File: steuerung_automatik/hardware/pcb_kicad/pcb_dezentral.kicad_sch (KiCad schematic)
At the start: 37 parts, among them J101 USB_C_Receptacle_USB2.0, J102 weidmueller_SL5.08HC-06-90, J103 weidmueller_SL5.08HC-10-90, SW101 SW_MEC_5E, SW102 SW_MEC_5E, U101 RP2040, U102 W25Q128JVS, U103 SP3485EN-L/TR, U104 AMS1117-3.3, Y101 Crystal_GND24_Small

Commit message: Schema dezentral komplett
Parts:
- removed C101, C102, C105, C106, C109, C110, C111, C112, C113, C114: 100n, Capacitor_SMD:C_0402_1005Metric_Pad0.74x0.62mm_HandSolder, symbol 00_project_library:C
- removed C103, C104: 1u, Capacitor_SMD:C_0402_1005Metric_Pad0.74x0.62mm_HandSolder, symbol 00_project_library:C
- removed C107, C108: 30p, Capacitor_SMD:C_0402_1005Metric, symbol 00_project_library:C
- removed C115, C116: 10u, Capacitor_SMD:C_0603_1608Metric, symbol 00_project_library:C
- removed D101: LED GREEN, 00_project_library:LED_0603_1608Metric, symbol 00_project_library:LED GREEN
- removed J101: USB_C_Receptacle_USB2.0, 00_project_library:USB_C_Receptacle_Palconn_UTC16-G, symbol 00_project_library:USB_C_Receptacle_USB2.0
- removed R101, R102: 5.1K, Resistor_SMD:R_0402_1005Metric_Pad0.72x0.64mm_HandSolder, symbol Device:R
- removed R103, R104: 27R, Resistor_SMD:R_0402_1005Metric_Pad0.72x0.64mm_HandSolder, symbol Device:R
- removed R105, R107: 10K, Resistor_SMD:R_0402_1005Metric_Pad0.72x0.64mm_HandSolder, symbol Device:R
- removed R106: 470R, Resistor_SMD:R_0402_1005Metric_Pad0.72x0.64mm_HandSolder, symbol Device:R
- removed R108: 1k, Resistor_SMD:R_0402_1005Metric_Pad0.72x0.64mm_HandSolder, symbol Device:R
- removed SW101, SW102: SW_MEC_5E, 00_project_library:SW_TS-1187A-B-A-B, symbol 00_project_library:SW_MEC_5E
- removed TP101: TestPoint, TestPoint:TestPoint_Pad_D2.5mm, symbol Connector:TestPoint
- removed U101: RP2040, 00_project_library:RP2040-QFN-56, symbol 00_project_library:RP2040
- removed U102: W25Q128JVS, 00_project_library:SOIC-8_5.23x5.23mm_P1.27mm, symbol 00_project_library:W25Q128JVS
- removed U104: AMS1117-3.3, 00_project_library:SOT-223-3_TabPin2, symbol 00_project_library:AMS1117-3.3
- removed Y101: Crystal_GND24_Small, 00_project_library:Crystal_SMD_3225-4Pin_3.2x2.5mm, symbol 00_project_library:Crystal_GND24_Small
- added C1: 4u7 50V, Diode_SMD:D_1206_3216Metric, symbol Device:C
- added C2, C3, C5, C6: 100n 50V, Diode_SMD:D_0805_2012Metric, symbol Device:C
- added C4: 10u 25V, Diode_SMD:D_0805_2012Metric, symbol Device:C
- added D1, D10, D11, D12, D13, D14, D15, D16, D19, D2, D20, D24, D25, D3, D4, D5, D6, D7, D8, D9: B5819W SL, Diode_SMD:D_SOD-123, symbol Device:D_Schottky
- added D17: SMBJ30A, Diode_SMD:D_SMA, symbol Diode:SMAJ64A
- added D18: LED WHITE, 00_project_library:LED_0603_1608Metric, symbol 00_project_library:LED WHITE
- added D21, D22, D23: SMBJ6.5CA, Diode_SMD:D_SMB, symbol Diode:SMAJ64CA
- added L1: 22uH, 00_project_library:L_MODBUS, symbol Device:L
- added Q1: AO3400A, Package_TO_SOT_SMD:SOT-23, symbol Transistor_FET:AO3400A
- added R1, R2, R3, R4, R5, R6, R7, R8: 4k7, Resistor_SMD:R_0402_1005Metric_Pad0.72x0.64mm_HandSolder, symbol Device:R
- added R10, R13: 10k, Resistor_SMD:R_0402_1005Metric_Pad0.72x0.64mm_HandSolder, symbol Device:R
- added R11: 100k, Resistor_SMD:R_0402_1005Metric_Pad0.72x0.64mm_HandSolder, symbol Device:R
- added R12: 56k, Resistor_SMD:R_0402_1005Metric_Pad0.72x0.64mm_HandSolder, symbol Device:R
- added R9: 470, Resistor_SMD:R_0402_1005Metric_Pad0.72x0.64mm_HandSolder, symbol Device:R
- added SW1: dip_switch_SPST16, 00_project_library:dip_switch_SPST16, symbol 00_project_library:dip_switch_SPST16
- added U2: AOZ1282CI, Package_TO_SOT_SMD:SOT-23-6, symbol Regulator_Switching:AOZ1282CI
- renumbered HOLDER101 to HOLDER1, J102 to J1, J103 to J2, U103 to U1
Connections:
- net +3V3: now also J2.9, C6.2, D1.1 (K), D11.1 (K), D13.1 (K), D15.1 (K), D3.1 (K), D5.1 (K), D7.1 (K), D9.1 (K), R1.1, R2.1, R3.1, R4.1, R5.1, R6.1, R7.1, R8.1, SW1.1-1, SW1.2-1, SW1.3-1, SW1.4-1, SW1.5-1, SW1.6-1, SW1.7-1, SW1.8-1
- net +5V: now also D25.1 (K)
- net GND: now also J1.3, J2.10, U1.5 (GND), C1.2, C2.2, C4.1, C5.1, C6.1, D10.2 (A), D12.2 (A), D14.2 (A), D16.2 (A), D17.2 (A2), D2.2 (A), D21.2 (A2), D23.1 (A1), D24.2 (A), D4.2 (A), D6.2 (A), D8.2 (A), Q1.2 (S), R10.2, R13.2, R9.2, U2.2 (GND)
- net MODBUS_RO: now reaches U1.1 (RO)
- net MODBUS_DE: now reaches U1.2 (~{RE})
- net MODBUS_DE: now also U1.3 (DE)
- net MODBUS_DI: now reaches U1.4 (DI)
- net 485_A: now reaches U1.6 (A)
- net 485_A: now also J1.1, D21.1 (A1), D22.2 (A2)
- net 485_B: now reaches U1.7 (B)
- net 485_B: now also J1.2, D22.1 (A1), D23.2 (A2)
- net +3.3V: now reaches U1.8 (VCC)
- net ds_0: now reaches J2.1
- net ds_0: now also D1.2 (A), D2.1 (K), R1.2
- net ds_1: now reaches J2.2
- net ds_1: now also D3.2 (A), D4.1 (K), R2.2
- net ds_2: now reaches J2.3
- net ds_2: now also D5.2 (A), D6.1 (K), R3.2
- net ds_3: now reaches J2.4
- net ds_3: now also D7.2 (A), D8.1 (K), R4.2
- net ds_4: now reaches J2.5
- net ds_4: now also D10.1 (K), D9.2 (A), R5.2
- net ds_5: now reaches J2.6
- net ds_5: now also D11.2 (A), D12.1 (K), R6.2
- net ds_6: now reaches J2.7
- net ds_6: now also D13.2 (A), D14.1 (K), R7.2
- net ds_7: now reaches J2.8
- net ds_7: now also D15.2 (A), D16.1 (K), R8.2
- net 485_24V: now reaches J1.4
- net 485_24V: now also J1.5, D17.1 (A1), D19.2 (A), D20.1 (K)
- net rel_n: now reaches J1.6
- net rel_n: now also D20.2 (A), Q1.3 (D)
- new net: C1.1, C2.1, D19.1 (K), R11.1, U2.5 (VIN)
- new net: R12.1, R13.1, U2.3 (FB)
- new net: D18.1 (K), R9.1
- new net: C4.2, C5.2, D25.2 (A), L1.2, R12.2
- new net: R11.2, U2.4 (EN)
- new net: C3.2, D24.1 (K), L1.1, U2.6 (LX)
- new net: C3.1, U2.1 (BST)
- new net modbus_addr_0: SW1.1
- new net modbus_addr_1: SW1.2
- new net modbus_addr_2: SW1.3
- new net modbus_addr_3: SW1.4
- new net modbus_addr_4: SW1.5
- new net modbus_addr_5: SW1.6
- new net modbus_addr_6: SW1.7
- new net modbus_addr_7: SW1.8
- new net rel: D18.2 (A), Q1.1 (G), R10.1
- no-connect marks 34 -> 0
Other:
- added sheet cpu (pcb_dezentral_cpu.kicad_sch)
- note added: "5.3V"
- note added: "Mechanics"
- note removed: "Bypass Capacitors"
- note removed: "C1, C2 = 2*CL - 2*Cs CL = 20pF, Cs can be ~5pF"
- note removed: "Crystal"
- note removed: "Flash Memory"
- note removed: "Main Regulator"
- note removed: "Make sure 27R are close to RP2040"
- note removed: "Mounting Hole"
- note removed: "Place 1uF close to pin 44"
- note removed: "Place 1uF close to pin 45"
- note removed: "Power LED"
- note removed: "RP2040"
- note removed: "Reset"
- note removed: "USB Type-C"
- title: Heizung Pünterswis - pcb_zentral -> Heizung Pünterswis - pcb_dezentral
- moved on the sheet: J1, J2, U1

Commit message: Schema dezentral komplett
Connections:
- net +3.3V is gone; now on net +3V3: U1.8 (VCC)
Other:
- moved on the sheet: C6, D10, D12, D14, D16, D17, D2, D4, D6, D8

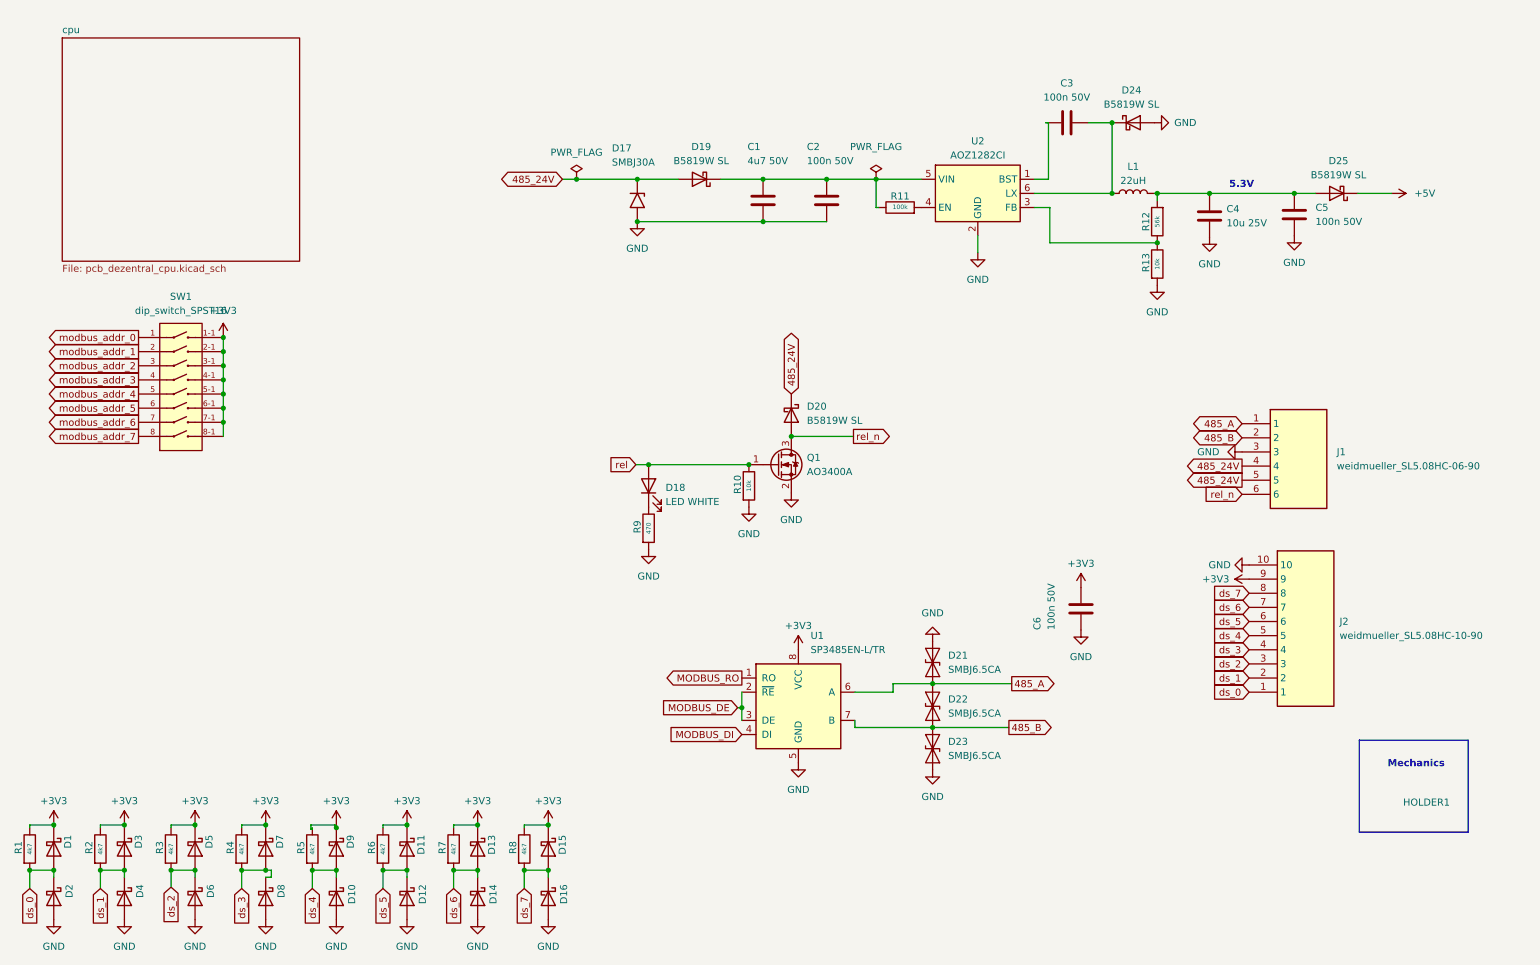
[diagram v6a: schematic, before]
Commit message: Schema bereinigt
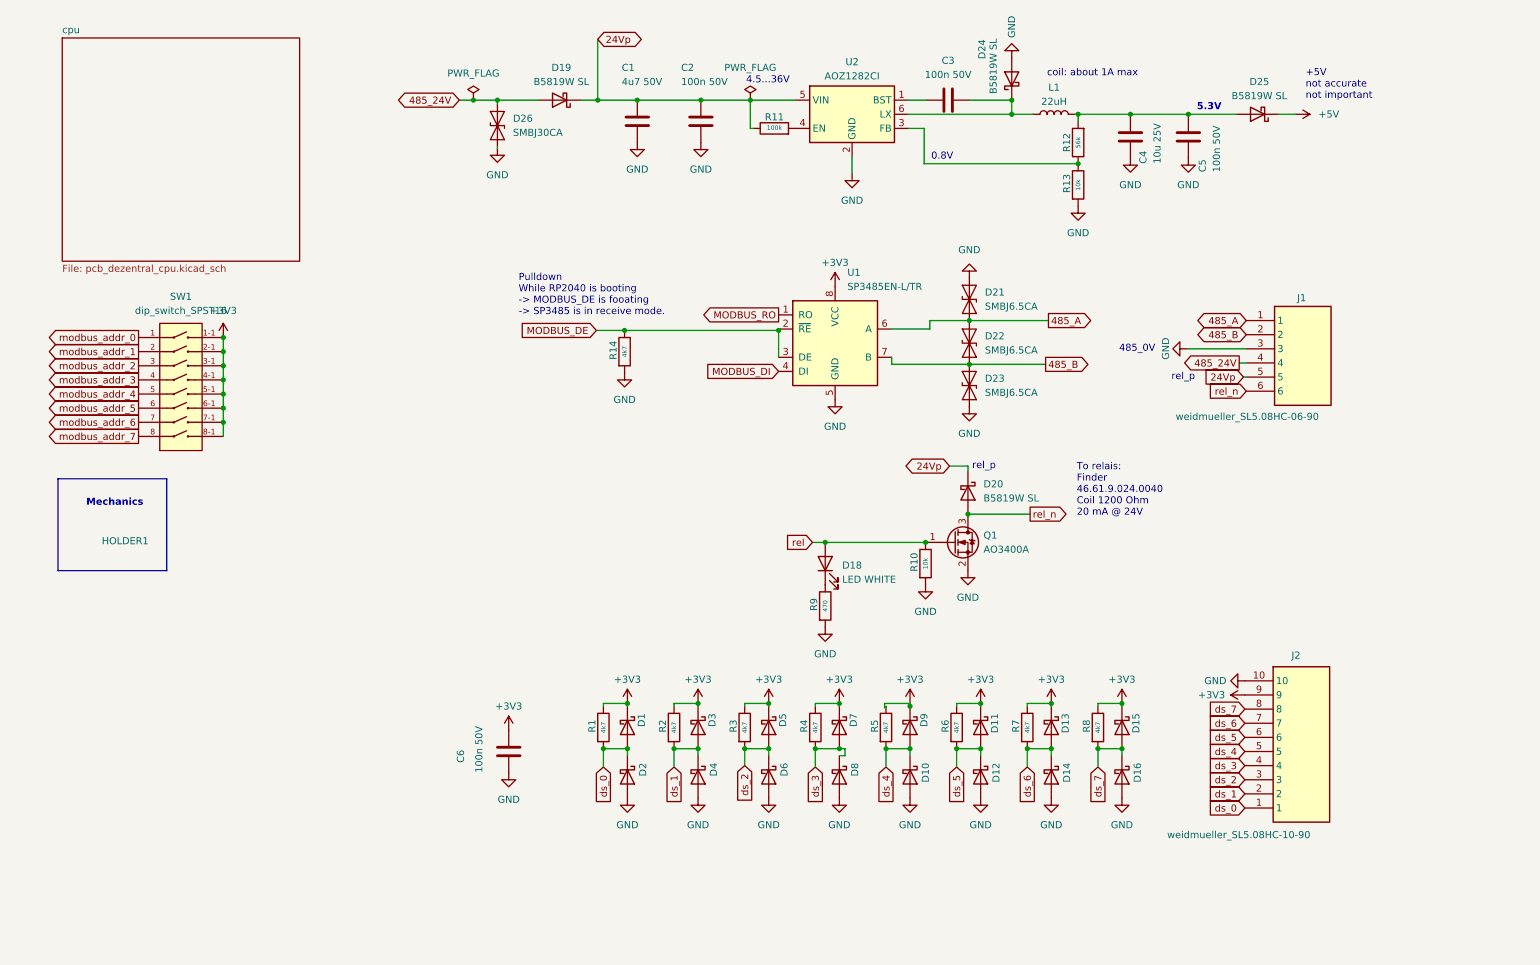
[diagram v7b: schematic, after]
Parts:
- removed D17: SMBJ30A, Diode_SMD:D_SMA, symbol Diode:SMAJ64A
- added D26: SMBJ30CA, Diode_SMD:D_SMB, symbol Diode:SMAJ64CA
- added R14: 4k7, Resistor_SMD:R_0402_1005Metric_Pad0.72x0.64mm_HandSolder, symbol Device:R
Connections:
- net 485_24V: now also D26.2 (A2); no longer D20.1 (K), J1.5
- net GND: now also D26.1 (A1), R14.2
- net MODBUS_DE: now also R14.1
- net 24Vp: now reaches C1.1, C2.1, D19.1 (K), R11.1, U2.5 (VIN)
- net 24Vp: now also D20.1 (K), J1.5
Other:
- note added: "+5V not accurate not important"
- note added: "0.8V"
- note added: "4.5...36V"
- note added: "485_0V"
- note added: "Pulldown While RP2040 is booting -> MODBUS_DE is fooating -> SP3485 is in receive mode."
- note added: "To relais: Finder 46.61.9.024.0040 Coil 1200 Ohm 20 mA @ 24V"
- note added: "coil: about 1A max"
- note added: "rel_p"
- moved on the sheet: C1, C2, C3, C4, C5, C6, D1, D10, D11, D12, D13, D14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

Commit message: Anpassungen von Peter
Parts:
- added D17: LED RED, 00_project_library:LED_0603_1608Metric, symbol 00_project_library:LED RED
- added D27: LED BLUE, 00_project_library:LED_0603_1608Metric, symbol 00_project_library:LED BLUE
- added R15, R16: 470R, Resistor_SMD:R_0402_1005Metric_Pad0.72x0.64mm_HandSolder, symbol Device:R
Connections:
- net GND: now also R15.1, R16.1
- new net: D17.1 (K), R15.2
- new net: D27.2 (A), R16.2
- new net modbus_led: D17.2 (A), D27.1 (K)
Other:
- note added: "Modbus LED"
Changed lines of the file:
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@@
     (stroke (width 0) (type default))
+  )
+  (wire (pts (xy 49.53 151.638) (xy 53.34 151.638))
+    (stroke (width 0) (type solid))
   )
   (wire (pts (xy 52.578 82.042) (xy 52.578 84.582))
@@
     (stroke (width 0) (type default))
   )
+  (wire (pts (xy 60.96 151.638) (xy 62.23 151.638))
+    (stroke (width 0) (type solid))
+  )
   (wire (pts (xy 52.578 74.422) (xy 52.578 76.962))
     (stroke (width 0) (type default))
@@
     (stroke (width 0) (type default))
   )
+  (wire (pts (xy 49.53 162.052) (xy 53.34 162.052))
+    (stroke (width 0) (type solid))
+  )
   (wire (pts (xy 101.854 40.132) (xy 101.854 40.386))
     (stroke (width 0) (type default))
@@
     (stroke (width 0) (type default))
   )
+  (wire (pts (xy 60.96 162.052) (xy 62.23 162.052))
+    (stroke (width 0) (type solid))
+  )
   (wire (pts (xy 179.578 71.374) (xy 186.69 71.374))
     (stroke (width 0) (type default))
@@
     (stroke (width 0) (type default))
   )
+  (wire (pts (xy 39.37 162.052) (xy 41.91 162.052))
+    (stroke (width 0) (type default))
+  )
   (wire (pts (xy 119.888 20.828) (xy 119.888 31.75))
     (stroke (width 0) (type default))
@@
     (stroke (width 0) (type default))
   )
+  (wire (pts (xy 39.37 151.638) (xy 41.91 151.638))
+    (stroke (width 0) (type default))
+  )
   (wire (pts (xy 52.578 79.502) (xy 52.578 82.042))
     (stroke (width 0) (type default))
@@
     (stroke (width 0) (type default))
   )
+  (rectangle (start 23.876 139.192) (end 69.088 165.608)
+    (stroke (width 0) (type default))
+    (fill (type none))
+  )
   (rectangle (start 22.86 99.822) (end 42.418 116.332)
     (stroke (width 0) (type default))
@@
   )
   (text "Mechanics" (at 27.94 104.902 0)
+    (effects (font (size 1.27 1.27) (thickness 0.254) bold) (justify left bottom))
+  )
+  (text "Modbus LED" (at 30.48 144.526 0)
     (effects (font (size 1.27 1.27) (thickness 0.254) bold) (justify left bottom))
   )
@@
   (text "0.8V" (at 179.832 42.672 0)
     (effects (font (size 1.27 1.27)) (justify left bottom))
+  )
+  (global_label "modbus_led" (shape output) (at 39.37 151.638 180) (fields_autoplaced)
+    (effects (font (size 1.27 1.27)) (justify right))
+    (property "Intersheetrefs" "${INTERSHEET_REFS}" (at 25.1019 151.638 0)
+      (effects (font (size 1.27 1.27)) (justify right) hide)
+    )
   )
   (global_label "modbus_addr_3" (shape output) (at 37.338 82.042 180) (fields_autoplaced)
@@
     )
   )
+  (global_label "modbus_led" (shape output) (at 39.37 162.052 180) (fields_autoplaced)
+    (effects (font (size 1.27 1.27)) (justify right))
+    (property "Intersheetrefs" "${INTERSHEET_REFS}" (at 25.1019 162.052 0)
+      (effects (font (size 1.27 1.27)) (justify right) hide)
+    )
+  )
   (global_label "modbus_addr_5" (shape output) (at 37.338 87.122 180) (fields_autoplaced)
     (effects (font (size 1.27 1.27)) (justify right))
@@
     )
   )
+  (symbol (lib_id "power:GND") (at 62.23 162.052 90) (unit 1)
+    (in_bom yes) (on_board yes) (dnp no)
+    (property "Reference" "#PWR042" (at 68.58 162.052 0)
+      (effects (font (size 0.8 0.8)) hide)
+    )
+    (property "Value" "GND" (at 65.8622 162.179 0)
+      (effects (font (size 0.8 0.8)))
+    )
+    (property "Footprint" "" (at 62.23 162.052 0)
+      (effects (font (size 0.8 0.8)) hide)
+    )
+    (property "Datasheet" "" (at 62.23 162.052 0)
+      (effects (font (size 0.8 0.8)) hide)
+    )
+    (pin "1")
+    (instances
+      (project "pcb_dezentral"
+        (path "/35c47459-45a7-4753-acae-c8b47e7575e1"
+          (reference "#PWR042") (unit 1)
+        )
+        (path "/35c47459-45a7-4753-acae-c8b47e7575e1/24d7d496-8920-4421-a637-0c9bf263a085"
+          (reference "#PWR0913") (unit 1)
+        )
+      )
+    )
+  )
   (symbol (lib_id "power:GND") (at 178.816 118.872 0) (unit 1)
     (in_bom yes) (on_board yes) (dnp no) (fields_autoplaced)
@@
         (path "/35c47459-45a7-4753-acae-c8b47e7575e1"
           (reference "#PWR020") (unit 1)
+        )
+      )
+    )
+  )
+  (symbol (lib_id "Device:R") (at 57.15 151.638 270) (unit 1)
+    (in_bom yes) (on_board yes) (dnp no)
+    (property "Reference" "R15" (at 57.15 153.67 90)
+      (effects (font (size 1.27 1.27)))
+    )
+    (property "Value" "470R" (at 57.15 151.7396 90)
+      (effects (font (size 0.8 0.8)))
+    )
+    (property "Footprint" "Resistor_SMD:R_0402_1005Metric_Pad0.72x0.64mm_HandSolder" (at 57.15 149.86 90)
+      (effects (font (size 1.27 1.27)) hide)
+    )
+    (property "Datasheet" "~" (at 57.15 151.638 0)
+      (effects (font (size 1.27 1.27)) hide)
+    )
+    (pin "1")
+    (pin "2")
+    (instances
+      (project "pcb_dezentral"
+        (path "/35c47459-45a7-4753-acae-c8b47e7575e1"
+          (reference "R15") (unit 1)
+        )
+        (path "/35c47459-45a7-4753-acae-c8b47e7575e1/24d7d496-8920-4421-a637-0c9bf263a085"
+          (reference "R905") (unit 1)
         )
       )
@@
         (path "/35c47459-45a7-4753-acae-c8b47e7575e1"
           (reference "#PWR014") (unit 1)
+        )
+      )
+    )
+  )
+  (symbol (lib_id "00_project_library:LED RED") (at 45.72 151.638 180) (unit 1)
+    (in_bom yes) (on_board yes) (dnp no) (fields_autoplaced)
+    (property "Reference" "D17" (at 47.3075 144.526 0)
+      (effects (font (size 1.27 1.27)))
+    )
+    (property "Value" "LED RED" (at 47.3075 147.066 0)
+      (effects (font (size 1.27 1.27)))
+    )
+    (property "Footprint" "00_project_library:LED_0603_1608Metric" (at 45.72 151.638 0)
+      (effects (font (size 1.27 1.27)) hide)
+    )
+    (property "Datasheet" "~" (at 45.72 151.638 0)
+      (effects (font (size 1.27 1.27)) hide)
+    )
+    (property "JLC" "C2286" (at 45.72 151.638 0)
+      (effects (font (size 1.27 1.27)) hide)
+    )
+    (pin "1")
+    (pin "2")
+    (instances
+      (project "pcb_dezentral"
+        (path "/35c47459-45a7-4753-acae-c8b47e7575e1"
+          (reference "D17") (unit 1)
         )
       )
@@
         (path "/35c47459-45a7-4753-acae-c8b47e7575e1"
           (reference "D1") (unit 1)
+        )
+      )
+    )
+  )
+  (symbol (lib_id "00_project_library:LED BLUE") (at 45.72 162.052 0) (unit 1)
+    (in_bom yes) (on_board yes) (dnp no) (fields_autoplaced)
+    (property "Reference" "D27" (at 44.1325 155.956 0)
+      (effects (font (size 1.27 1.27)))
+    )
+    (property "Value" "LED BLUE" (at 44.1325 158.496 0)
+      (effects (font (size 1.27 1.27)))
+    )
+    (property "Footprint" "00_project_library:LED_0603_1608Metric" (at 45.72 162.052 0)
+      (effects (font (size 1.27 1.27)) hide)
+    )
+    (property "Datasheet" "~" (at 45.72 162.052 0)
+      (effects (font (size 1.27 1.27)) hide)
+    )
+    (property "JLC" "C189307" (at 45.72 162.052 0)
+      (effects (font (size 1.27 1.27)) hide)
+    )
+    (pin "1")
+    (pin "2")
+    (instances
+      (project "pcb_dezentral"
+        (path "/35c47459-45a7-4753-acae-c8b47e7575e1"
+          (reference "D27") (unit 1)
         )
       )
@@
         )
       )
+    )
+  )
+  (symbol (lib_id "power:GND") (at 62.23 151.638 90) (unit 1)
+    (in_bom yes) (on_board yes) (dnp no)
+    (property "Reference" "#PWR041" (at 68.58 151.638 0)
+      (effects (font (size 0.8 0.8)) hide)
+    )
+    (property "Value" "GND" (at 65.8622 151.765 0)
+      (effects (font (size 0.8 0.8)))
+    )
+    (property "Footprint" "" (at 62.23 151.638 0)
+      (effects (font (size 0.8 0.8)) hide)
+    )
+    (property "Datasheet" "" (at 62.23 151.638 0)
+      (effects (font (size 0.8 0.8)) hide)
+    )
+    (pin "1")
+    (instances
+      (project "pcb_dezentral"
+        (path "/35c47459-45a7-4753-acae-c8b47e7575e1"
+          (reference "#PWR041") (unit 1)
+        )
+        (path "/35c47459-45a7-4753-acae-c8b47e7575e1/24d7d496-8920-4421-a637-0c9bf263a085"
+          (reference "#PWR0913") (unit 1)
+        )
+      )
+    )
+  )
+  (symbol (lib_id "Device:R") (at 57.15 162.052 270) (unit 1)
+    (in_bom yes) (on_board yes) (dnp no)
+    (property "Reference" "R16" (at 57.15 164.084 90)
+      (effects (font (size 1.27 1.27)))
+    )
+    (property "Value" "470R" (at 57.15 162.1536 90)
+      (effects (font (size 0.8 0.8)))
+    )
+    (property "Footprint" "Resistor_SMD:R_0402_1005Metric_Pad0.72x0.64mm_HandSolder" (at 57.15 160.274 90)
+      (effects (font (size 1.27 1.27)) hide)
+    )
+    (property "Datasheet" "~" (at 57.15 162.052 0)
+      (effects (font (size 1.27 1.27)) hide)
+    )
+    (pin "1")
+    (pin "2")
+    (instances
+      (project "pcb_dezentral"
+        (path "/35c47459-45a7-4753-acae-c8b47e7575e1"
+          (reference "R16") (unit 1)
+        )
+        (path "/35c47459-45a7-4753-acae-c8b47e7575e1/24d7d496-8920-4421-a637-0c9bf263a085"
+          (reference "R905") (unit 1)
+        )
+      )
